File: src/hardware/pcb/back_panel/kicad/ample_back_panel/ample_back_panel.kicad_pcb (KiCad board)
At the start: 2 copper layers, 103 x 30.5 mm, 0 parts

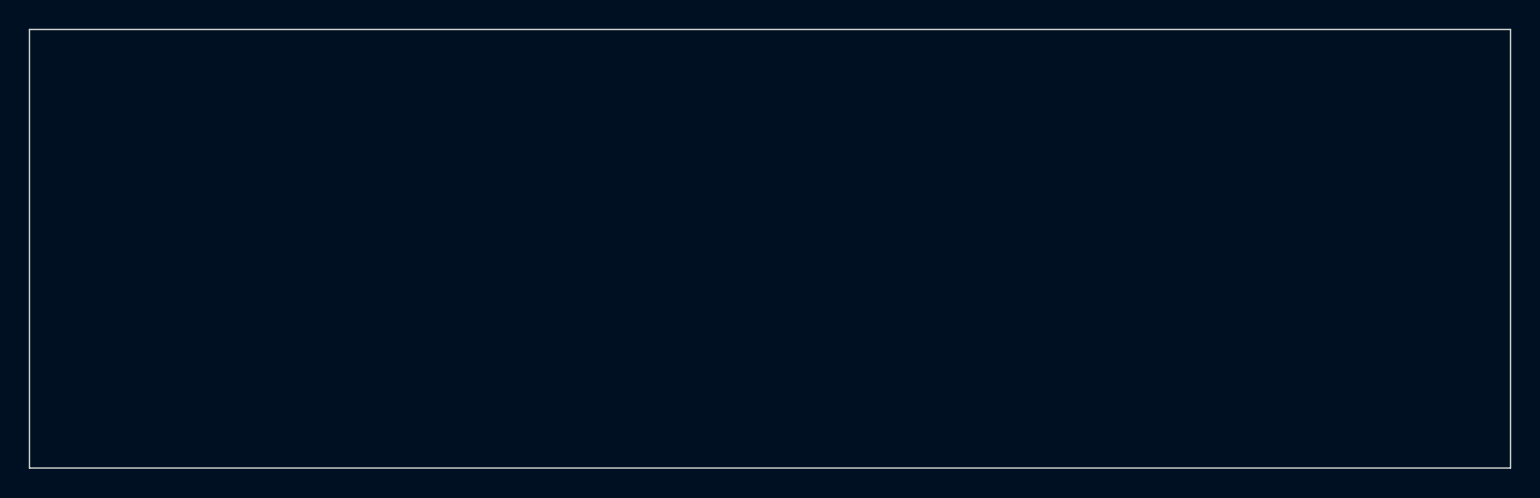
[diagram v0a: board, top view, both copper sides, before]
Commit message: init board shape
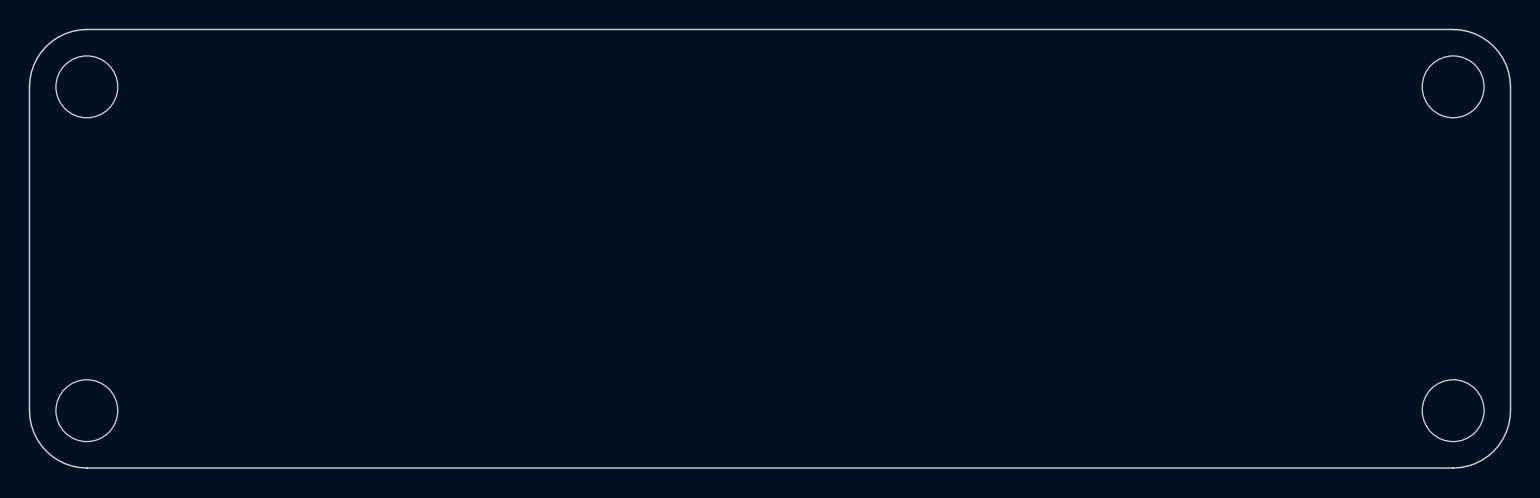
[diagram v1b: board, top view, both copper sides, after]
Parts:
- added H1: MountingHole, MountingHole:MountingHole_4.3mm_M4, F.Cu at (114.0, 103.5)
- added H2: MountingHole, MountingHole:MountingHole_4.3mm_M4, F.Cu at (209.0, 103.5)
- added H3: MountingHole, MountingHole:MountingHole_4.3mm_M4, F.Cu at (209.0, 126.0)
- added H4: MountingHole, MountingHole:MountingHole_4.3mm_M4, F.Cu at (114.0, 126.0)
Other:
- outline, holes or cut-outs redrawn
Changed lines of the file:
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@@
   )
   (net 0 "")
-  (gr_line (start 110 99.5) (end 213 99.5)
+  (footprint "MountingHole:MountingHole_4.3mm_M4" (layer "F.Cu")
+    (at 113.99 103.49)
+    (descr "Mounting Hole 4.3mm, no annular, M4")
+    (tags "mounting hole 4.3mm no annular m4")
+    (property "Sheetfile" "ample_back_panel.kicad_sch")
+    (property "Sheetname" "")
+    (property "ki_description" "Mounting Hole without connection")
+    (property "ki_keywords" "mounting hole")
+    (attr exclude_from_pos_files)
+    (fp_text reference "H1" (at 0 -5.3) (layer "F.SilkS") hide
+        (effects (font (size 1 1) (thickness 0.15)))
+    )
+    (fp_text value "MountingHole" (at 0 5.3) (layer "F.Fab")
+        (effects (font (size 1 1) (thickness 0.15)))
+    )
+    (fp_text user "${REFERENCE}" (at 0 0) (layer "F.Fab")
+        (effects (font (size 1 1) (thickness 0.15)))
+    )
+    (fp_circle (center 0 0) (end 4.3 0)
+      (stroke (width 0.15) (type solid)) (fill none) (layer "Cmts.User"))
+    (fp_circle (center 0 0) (end 4.55 0)
+      (stroke (width 0.05) (type solid)) (fill none) (layer "F.CrtYd"))
+    (pad "" np_thru_hole circle (at 0 0) (size 4.3 4.3) (drill 4.3) (layers "*.Cu" "*.Mask"))
+  )
+  (footprint "MountingHole:MountingHole_4.3mm_M4" (layer "F.Cu")
+    (at 113.99 126.01)
+    (descr "Mounting Hole 4.3mm, no annular, M4")
+    (tags "mounting hole 4.3mm no annular m4")
+    (property "Sheetfile" "ample_back_panel.kicad_sch")
+    (property "Sheetname" "")
+    (property "ki_description" "Mounting Hole without connection")
+    (property "ki_keywords" "mounting hole")
+    (attr exclude_from_pos_files)
+    (fp_text reference "H4" (at 0 -5.3) (layer "F.SilkS") hide
+        (effects (font (size 1 1) (thickness 0.15)))
+    )
+    (fp_text value "MountingHole" (at 0 5.3) (layer "F.Fab")
+        (effects (font (size 1 1) (thickness 0.15)))
+    )
+    (fp_text user "${REFERENCE}" (at 0 0) (layer "F.Fab")
+        (effects (font (size 1 1) (thickness 0.15)))
+    )
+    (fp_circle (center 0 0) (end 4.3 0)
+      (stroke (width 0.15) (type solid)) (fill none) (layer "Cmts.User"))
+    (fp_circle (center 0 0) (end 4.55 0)
+      (stroke (width 0.05) (type solid)) (fill none) (layer "F.CrtYd"))
+    (pad "" np_thru_hole circle (at 0 0) (size 4.3 4.3) (drill 4.3) (layers "*.Cu" "*.Mask"))
+  )
+  (footprint "MountingHole:MountingHole_4.3mm_M4" (layer "F.Cu")
+    (at 209.01 126.01)
+    (descr "Mounting Hole 4.3mm, no annular, M4")
+    (tags "mounting hole 4.3mm no annular m4")
+    (property "Sheetfile" "ample_back_panel.kicad_sch")
+    (property "Sheetname" "")
+    (property "ki_description" "Mounting Hole without connection")
+    (property "ki_keywords" "mounting hole")
+    (attr exclude_from_pos_files)
+    (fp_text reference "H3" (at 0 -5.3) (layer "F.SilkS") hide
+        (effects (font (size 1 1) (thickness 0.15)))
+    )
+    (fp_text value "MountingHole" (at 0 5.3) (layer "F.Fab")
+        (effects (font (size 1 1) (thickness 0.15)))
+    )
+    (fp_text user "${REFERENCE}" (at 0 0) (layer "F.Fab")
+        (effects (font (size 1 1) (thickness 0.15)))
+    )
+    (fp_circle (center 0 0) (end 4.3 0)
+      (stroke (width 0.15) (type solid)) (fill none) (layer "Cmts.User"))
+    (fp_circle (center 0 0) (end 4.55 0)
+      (stroke (width 0.05) (type solid)) (fill none) (layer "F.CrtYd"))
+    (pad "" np_thru_hole circle (at 0 0) (size 4.3 4.3) (drill 4.3) (layers "*.Cu" "*.Mask"))
+  )
+  (footprint "MountingHole:MountingHole_4.3mm_M4" (layer "F.Cu")
+    (at 209.01 103.49)
+    (descr "Mounting Hole 4.3mm, no annular, M4")
+    (tags "mounting hole 4.3mm no annular m4")
+    (property "Sheetfile" "ample_back_panel.kicad_sch")
+    (property "Sheetname" "")
+    (property "ki_description" "Mounting Hole without connection")
+    (property "ki_keywords" "mounting hole")
+    (attr exclude_from_pos_files)
+    (fp_text reference "H2" (at 0 -5.3) (layer "F.SilkS") hide
+        (effects (font (size 1 1) (thickness 0.15)))
+    )
+    (fp_text value "MountingHole" (at 0 5.3) (layer "F.Fab")
+        (effects (font (size 1 1) (thickness 0.15)))
+    )
+    (fp_text user "${REFERENCE}" (at 0 0) (layer "F.Fab")
+        (effects (font (size 1 1) (thickness 0.15)))
+    )
+    (fp_circle (center 0 0) (end 4.3 0)
+      (stroke (width 0.15) (type solid)) (fill none) (layer "Cmts.User"))
+    (fp_circle (center 0 0) (end 4.55 0)
+      (stroke (width 0.05) (type solid)) (fill none) (layer "F.CrtYd"))
+    (pad "" np_thru_hole circle (at 0 0) (size 4.3 4.3) (drill 4.3) (layers "*.Cu" "*.Mask"))
+  )
+  (gr_arc (start 110 103.5) (mid 111.171573 100.671573) (end 114 99.5)
     (stroke (width 0.1) (type default)) (layer "Edge.Cuts"))
-  (gr_line (start 213 99.5) (end 213 130)
+  (gr_arc (start 114 130) (mid 111.171573 128.828427) (end 110 126)
     (stroke (width 0.1) (type default)) (layer "Edge.Cuts"))
-  (gr_line (start 110 130) (end 110 99.5)
+  (gr_line (start 114 99.5) (end 209 99.5)
     (stroke (width 0.1) (type default)) (layer "Edge.Cuts"))
-  (gr_line (start 213 130) (end 110 130)
+  (gr_arc (start 209 99.5) (mid 211.828427 100.671573) (end 213 103.5)
+    (stroke (width 0.1) (type default)) (layer "Edge.Cuts"))
+  (gr_line (start 213 103.5) (end 213 126)
+    (stroke (width 0.1) (type default)) (layer "Edge.Cuts"))
+  (gr_line (start 110 126) (end 110 103.5)
+    (stroke (width 0.1) (type default)) (layer "Edge.Cuts"))
+  (gr_line (start 209 130) (end 114 130)
+    (stroke (width 0.1) (type default)) (layer "Edge.Cuts"))
+  (gr_arc (start 213 126) (mid 211.828427 128.828427) (end 209 130)
     (stroke (width 0.1) (type default)) (layer "Edge.Cuts"))
 )
